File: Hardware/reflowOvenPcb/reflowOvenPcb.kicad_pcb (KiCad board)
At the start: 2 copper layers, 4 parts, among them J1 ISP, U1 ATmega328-M, U2 DM-OLED096-636

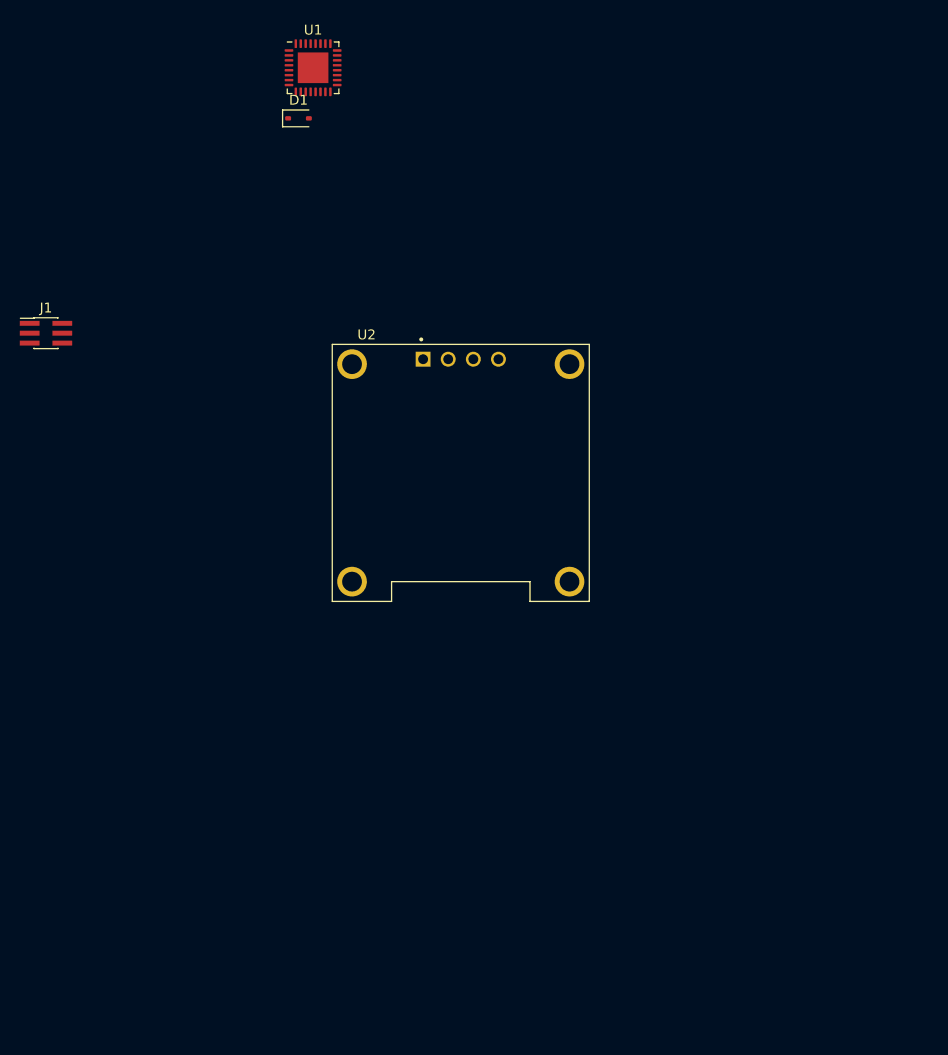
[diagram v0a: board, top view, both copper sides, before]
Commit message: Added multiple libraris, and place all the components
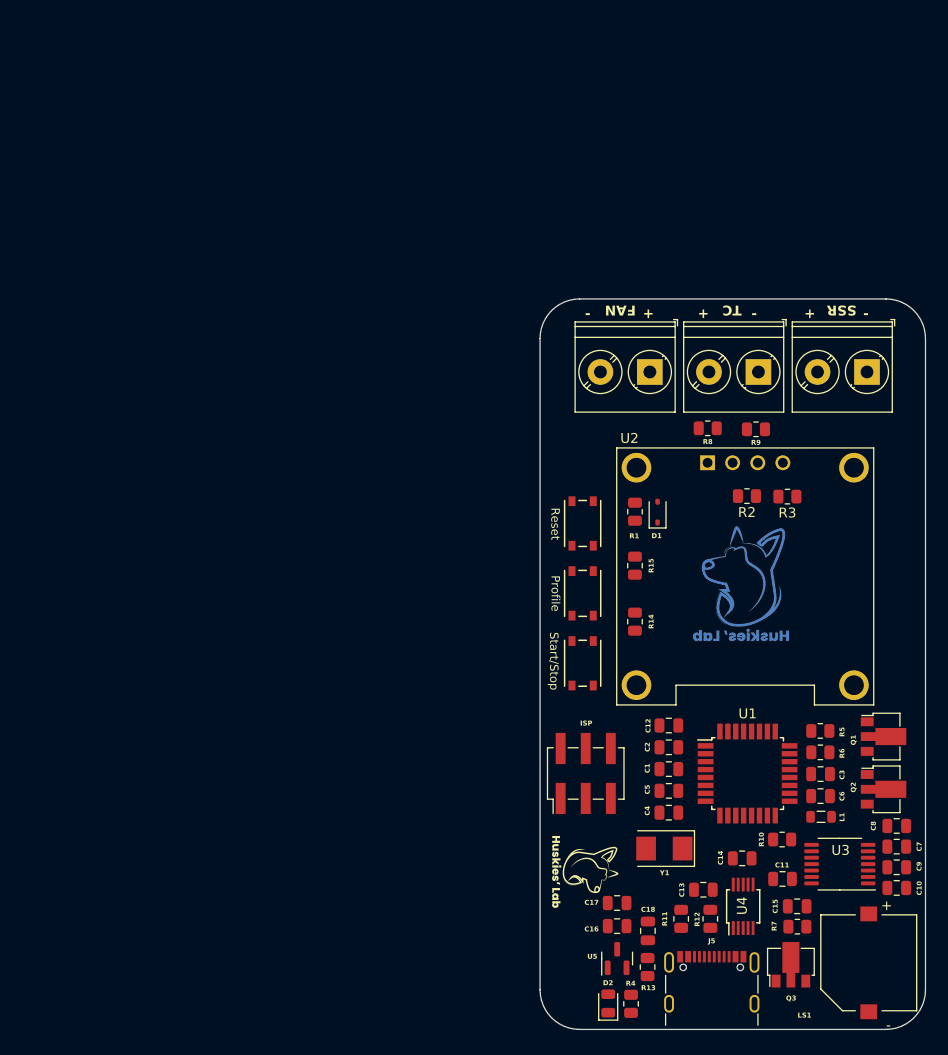
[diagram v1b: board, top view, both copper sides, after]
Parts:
- added C1: 100nF, Capacitor_SMD:C_0805_2012Metric, F.Cu at (140.1, 114.5)
- added C10: 100nF, Capacitor_SMD:C_0805_2012Metric, F.Cu at (163.1, 126.5)
- added C11: 100nF, Capacitor_SMD:C_0805_2012Metric, F.Cu at (151.6, 125.6)
- added C12: 10nF, Capacitor_SMD:C_0805_2012Metric, F.Cu at (140.1, 110.1)
- added C13: 100nF, Capacitor_SMD:C_0805_2012Metric, F.Cu at (143.6, 126.7)
- added C14: 100nF, Capacitor_SMD:C_0805_2012Metric, F.Cu at (147.5, 123.5)
- added C15: 100nF, Capacitor_SMD:C_0805_2012Metric, F.Cu at (153.1, 128.3)
- added C16: 100nF, Capacitor_SMD:C_0805_2012Metric, F.Cu at (134.9, 130.3)
- added C17: 10 uF 16V, Capacitor_SMD:C_0805_2012Metric, F.Cu at (134.9, 128.0)
- added C18: 10 uF 16V, Capacitor_SMD:C_0805_2012Metric, F.Cu at (138.0, 130.8)
- added C2: 100nF, Capacitor_SMD:C_0805_2012Metric, F.Cu at (140.1, 112.3)
- added C3: 100nF, Capacitor_SMD:C_0805_2012Metric, F.Cu at (155.4, 115.0)
- added C4: 10pF, Capacitor_SMD:C_0805_2012Metric, F.Cu at (140.1, 118.9)
- added C5: 10pF, Capacitor_SMD:C_0805_2012Metric, F.Cu at (140.1, 116.7)
- added C6: 100nF, Capacitor_SMD:C_0805_2012Metric, F.Cu at (155.4, 117.2)
- added C7: 10nF, Capacitor_SMD:C_0805_2012Metric, F.Cu at (163.1, 122.3)
- added C8: 100nF, Capacitor_SMD:C_0805_2012Metric, F.Cu at (163.1, 120.2)
- added C9: 10nF, Capacitor_SMD:C_0805_2012Metric, F.Cu at (163.1, 124.4)
- added D2: LED, LED_SMD:LED_0805_2012Metric, F.Cu at (134.0, 138.2)
- added Fan: Fan_output, TerminalBlock_Phoenix:TerminalBlock_Phoenix_PT-1,5-2-5.0-H_1x02_P5.00mm_Horizontal, F.Cu at (138.2, 74.3)
- added J5: USB_C_Receptacle_USB2.0, Connector_USB:USB_C_Receptacle_GCT_USB4105-xx-A_16P_TopMnt_Horizontal, F.Cu at (144.4, 137.1)
- added L1: L, Inductor_SMD:L_0805_2012Metric, F.Cu at (155.5, 119.3)
- added LS1: Buzzer, Buzzer_SMD:CUI_CMI-9705-0580-SMT-TR, F.Cu at (160.3, 134.1)
- added Profile: Perfil, SPST_Button_SMD:SW4_PTS815 SJM 250 SMTR LFS_CNK, F.Cu at (131.4, 96.7)
- added Q1: 2N3904, Package_TO_SOT_SMD:SOT-89-3, F.Cu at (162.1, 111.2)
- added Q2: 2N3904, Package_TO_SOT_SMD:SOT-89-3, F.Cu at (162.1, 116.5)
- added Q3: 2N3904, Package_TO_SOT_SMD:SOT-89-3, F.Cu at (152.4, 134.0)
- added R1: 10K, Resistor_SMD:R_0805_2012Metric, F.Cu at (136.7, 88.4)
- added R10: 10K, Resistor_SMD:R_0805_2012Metric, F.Cu at (151.6, 121.6)
- added R11: 5.11K, Resistor_SMD:R_0805_2012Metric, F.Cu at (141.3, 129.6)
- added R12: 5.11K, Resistor_SMD:R_0805_2012Metric, F.Cu at (144.3, 129.6)
- added R13: 1M, Resistor_SMD:R_0805_2012Metric, F.Cu at (137.9, 134.5)
- added R14: 2.2K, Resistor_SMD:R_0805_2012Metric, F.Cu at (136.7, 99.6)
- added R15: 2.2K, Resistor_SMD:R_0805_2012Metric, F.Cu at (136.7, 93.9)
- added R2: 2.2K, Resistor_SMD:R_0805_2012Metric, F.Cu at (148.0, 86.9)
- added R3: 2.2K, Resistor_SMD:R_0805_2012Metric, F.Cu at (152.1, 86.9)
- added R4: 2.2K, Resistor_SMD:R_0805_2012Metric, F.Cu at (136.3, 138.2)
- added R5: 53K5, Resistor_SMD:R_0805_2012Metric, F.Cu at (155.4, 110.6)
- added R6: 53K5, Resistor_SMD:R_0805_2012Metric, F.Cu at (155.4, 112.8)
- added R7: 27K, Resistor_SMD:R_0805_2012Metric, F.Cu at (153.1, 130.4)
- added R8: 100R, Resistor_SMD:R_0805_2012Metric, F.Cu at (144.0, 80.0)
- added R9: 100R, Resistor_SMD:R_0805_2012Metric, F.Cu at (148.9, 80.1)
- added REF**: Logo_F, Symbol:Logo_F, F.Cu at (132.2, 124.6)
- added REF**: LogoHlCooper, LogoCopper:LogoHlCooper, F.Cu at (147.8, 95.0)
- added Reset: RST_Button, SPST_Button_SMD:SW4_PTS815 SJM 250 SMTR LFS_CNK, F.Cu at (131.4, 89.6)
- added SRR: SSR_Output, TerminalBlock_Phoenix:TerminalBlock_Phoenix_PT-1,5-2-5.0-H_1x02_P5.00mm_Horizontal, F.Cu at (160.1, 74.3)
- added Start/Stop: Start/Stop, SPST_Button_SMD:SW4_PTS815 SJM 250 SMTR LFS_CNK, F.Cu at (131.4, 103.8)
- added TC: Thermocouple, TerminalBlock_Phoenix:TerminalBlock_Phoenix_PT-1,5-2-5.0-H_1x02_P5.00mm_Horizontal, F.Cu at (149.2, 74.3)
- added U3: MAX31856, Package_SO:TSSOP-14_4.4x5mm_P0.65mm, F.Cu at (157.4, 124.1)
- added U4: CH340E, Package_SO:MSOP-10_3x3mm_P0.5mm, F.Cu at (147.6, 128.3)
- added U5: MCP1700x-330xxTT, Package_TO_SOT_SMD:SOT-23, F.Cu at (134.9, 133.6)
- added Y1: 8Mhz, Crystal:Crystal_SMD_5032-2Pin_5.0x3.2mm, F.Cu at (139.6, 122.5)
- ISP: renamed from J1; footprint Connector_PinHeader_1.00mm:PinHeader_2x03_P1.00mm_Vertical_SMD -> Connector_PinHeader_2.54mm:PinHeader_2x03_P2.54mm_Vertical_SMD
- U1: footprint Package_DFN_QFN:QFN-32-1EP_5x5mm_P0.5mm_EP3.1x3.1mm -> Package_QFP:TQFP-32_7x7mm_P0.8mm
- U2: footprint OLED_SSD1306:MODULE_DM-OLED096-636 -> Oled_096:MODULE_DM-OLED096-636
- moved U1 83.8 mm to (148.1, 114.9)
- moved ISP 70.5 mm to (131.7, 114.9), turned to 90 degrees
- moved D1 53.9 mm to (139.0, 88.5), turned to 90 degrees
- moved U2 30.6 mm to (147.8, 95.0)
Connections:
- U2 pad 1: unconnected-(U2-GND-Pad1) -> GND
- U2 pad 2: unconnected-(U2-VCC_IN-Pad2) -> +3.3V
- U2 pad 3: unconnected-(U2-SCL-Pad3) -> /SCL
- U2 pad 4: unconnected-(U2-SDA-Pad4) -> /SDA
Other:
- board outline added: 39 x 73.9 mm
- board text added: "+"
- board text added: "-"
- board text added: "FAN"
- board text added: "SSR"
- board text added: "TC"

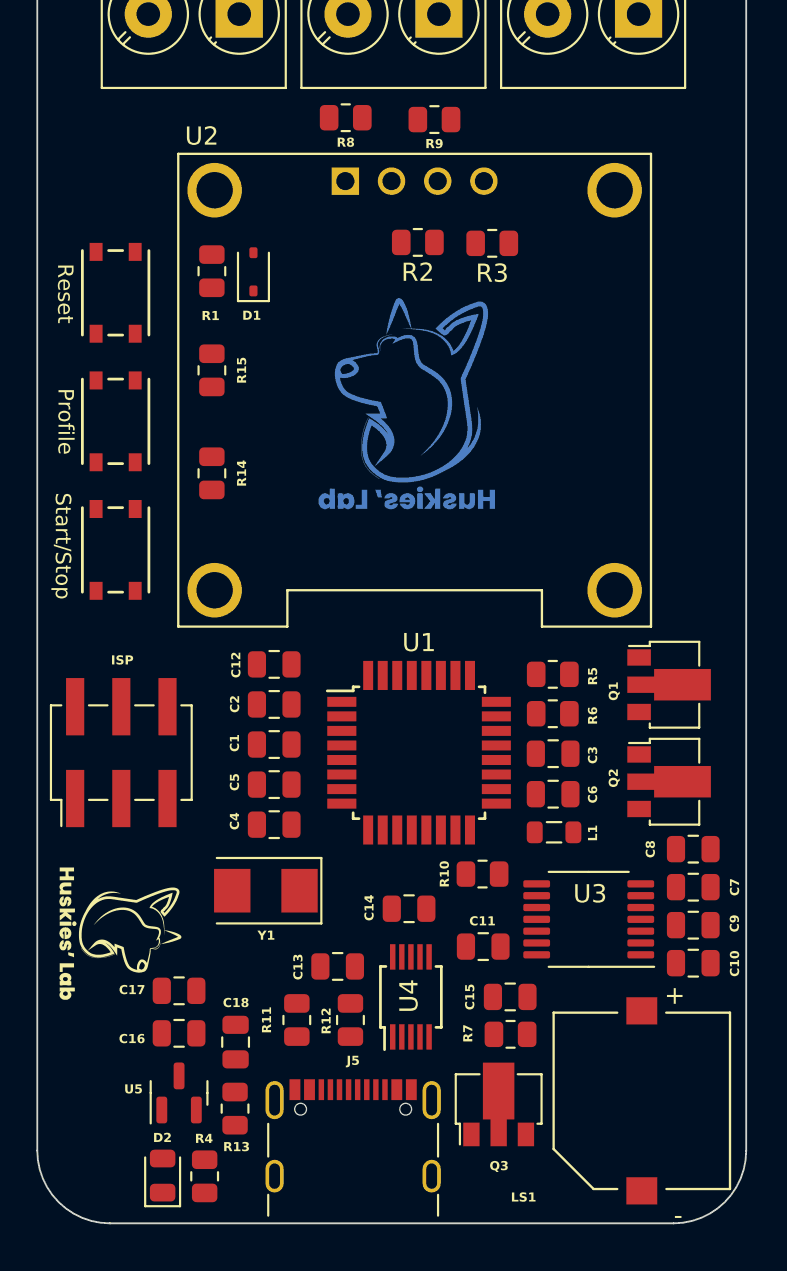
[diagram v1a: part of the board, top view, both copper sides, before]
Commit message: modified the layout of the board, and made some placement of the components
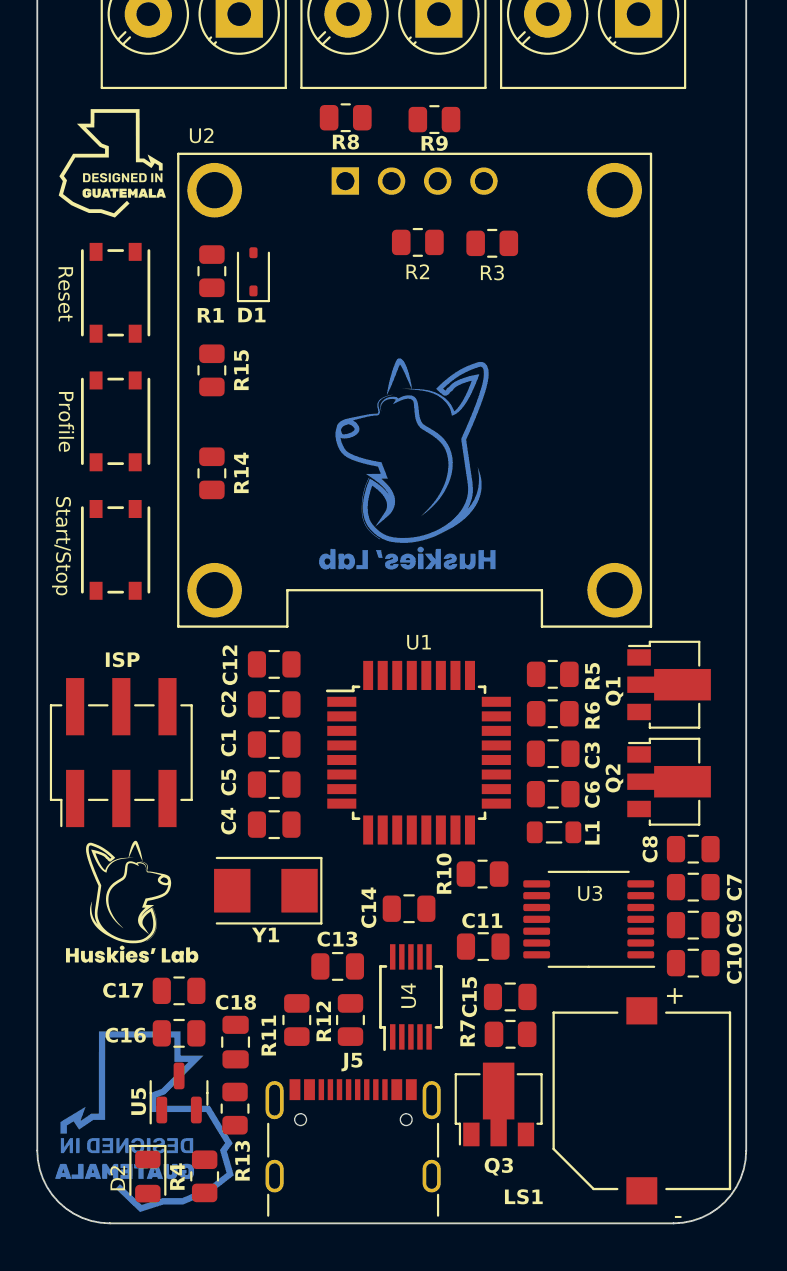
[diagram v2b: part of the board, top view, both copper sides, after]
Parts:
- added G***: LOGO, LOGO, F.Cu at (131.2, 82.5)
- added G***: LOGO, LOGO, F.Cu at (133.7, 135.2)
- moved REF** 3.32 mm to (147.9, 98.3)
- moved REF** 2.01 mm to (132.0, 122.6), turned to 0 degrees
- moved D2 0.81 mm to (133.1, 138.2), turned to -90 degrees
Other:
- board text added: "Designed by Alfonso Pinzon"
- board text added: "V1.0.0"
